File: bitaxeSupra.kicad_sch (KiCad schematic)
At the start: 20 parts, among them J1 54-00164

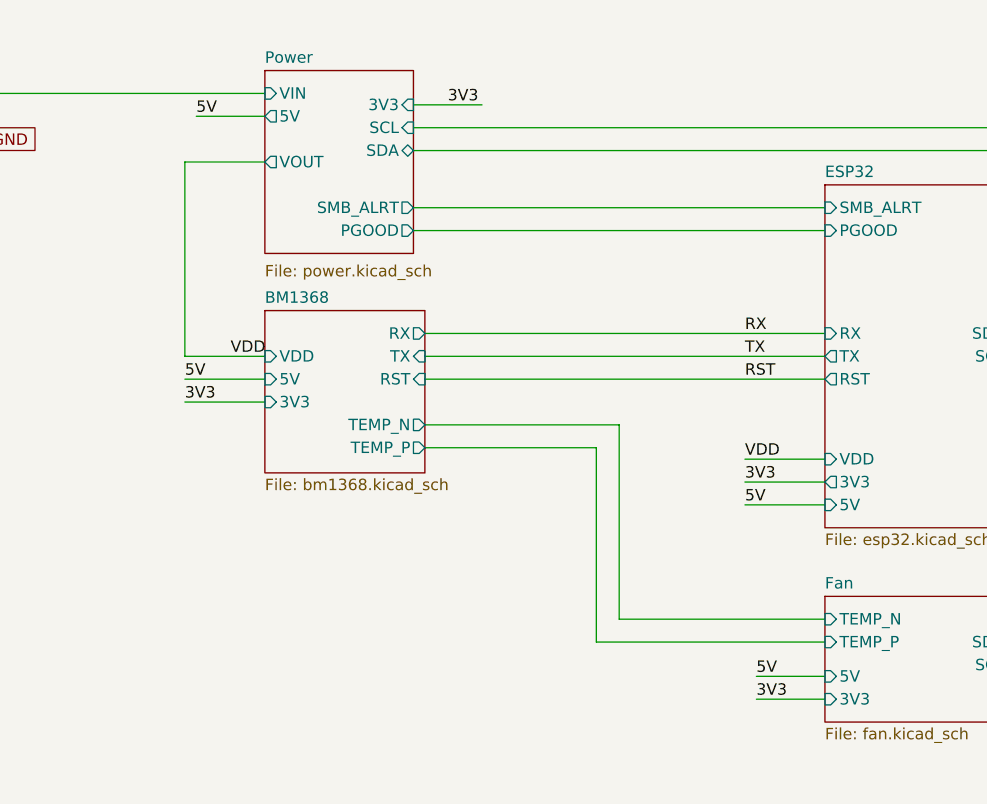
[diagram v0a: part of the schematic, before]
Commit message: changed 1.8V LDO to 1.2V LDO and 25MHz OSC to 1.2V model for #63
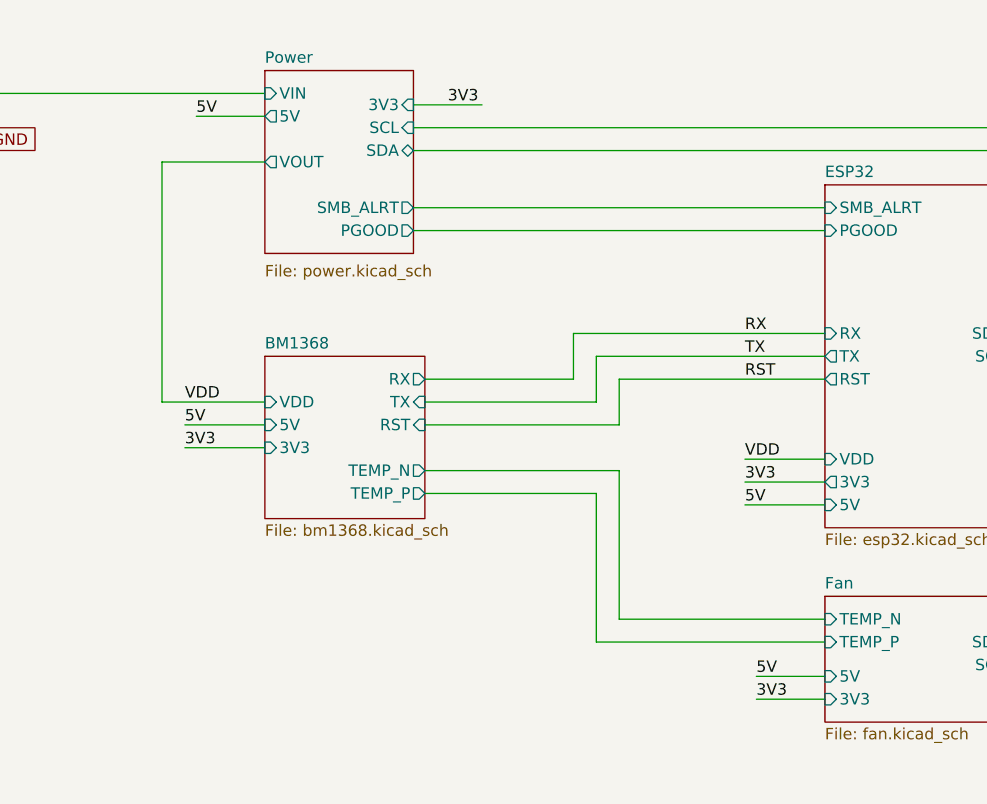
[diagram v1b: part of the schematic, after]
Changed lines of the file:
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@@
 	(wire
 		(pts
-			(xy 130.81 72.39) (xy 175.26 72.39)
+			(xy 147.32 74.93) (xy 147.32 69.85)
+		)
+		(stroke
+			(width 0)
+			(type default)
+		)
+	)
+	(wire
+		(pts
+			(xy 130.81 77.47) (xy 149.86 77.47)
 		)
 		(stroke
@@
 	(wire
 		(pts
+			(xy 152.4 74.93) (xy 175.26 74.93)
+		)
+		(stroke
+			(width 0)
+			(type default)
+		)
+	)
+	(wire
+		(pts
 			(xy 129.54 49.53) (xy 209.55 49.53)
 		)
@@
 	(wire
 		(pts
+			(xy 152.4 80.01) (xy 152.4 74.93)
+		)
+		(stroke
+			(width 0)
+			(type default)
+		)
+	)
+	(wire
+		(pts
 			(xy 35.56 163.83) (xy 35.56 171.45)
 		)
@@
 	(wire
 		(pts
-			(xy 104.14 77.47) (xy 113.03 77.47)
-		)
-		(stroke
-			(width 0)
-			(type default)
-		)
-	)
-	(wire
-		(pts
-			(xy 130.81 69.85) (xy 175.26 69.85)
+			(xy 104.14 82.55) (xy 113.03 82.55)
+		)
+		(stroke
+			(width 0)
+			(type default)
+		)
+	)
+	(wire
+		(pts
+			(xy 130.81 74.93) (xy 147.32 74.93)
 		)
 		(stroke
@@
 	(wire
 		(pts
-			(xy 104.14 72.39) (xy 104.14 50.8)
+			(xy 101.6 77.47) (xy 101.6 50.8)
+		)
+		(stroke
+			(width 0)
+			(type default)
+		)
+	)
+	(wire
+		(pts
+			(xy 130.81 85.09) (xy 152.4 85.09)
+		)
+		(stroke
+			(width 0)
+			(type default)
+		)
+	)
+	(wire
+		(pts
+			(xy 149.86 77.47) (xy 149.86 72.39)
+		)
+		(stroke
+			(width 0)
+			(type default)
+		)
+	)
+	(wire
+		(pts
+			(xy 196.85 106.68) (xy 207.01 106.68)
+		)
+		(stroke
+			(width 0)
+			(type default)
+		)
+	)
+	(wire
+		(pts
+			(xy 104.14 80.01) (xy 113.03 80.01)
+		)
+		(stroke
+			(width 0)
+			(type default)
+		)
+	)
+	(wire
+		(pts
+			(xy 149.86 87.63) (xy 130.81 87.63)
+		)
+		(stroke
+			(width 0)
+			(type default)
+		)
+	)
+	(wire
+		(pts
+			(xy 209.55 104.14) (xy 209.55 69.85)
+		)
+		(stroke
+			(width 0)
+			(type default)
+		)
+	)
+	(wire
+		(pts
+			(xy 129.54 58.42) (xy 175.26 58.42)
+		)
+		(stroke
+			(width 0)
+			(type default)
+		)
+	)
+	(wire
+		(pts
+			(xy 167.64 107.95) (xy 175.26 107.95)
+		)
+		(stroke
+			(width 0)
+			(type default)
+		)
+	)
+	(wire
+		(pts
+			(xy 129.54 55.88) (xy 175.26 55.88)
+		)
+		(stroke
+			(width 0)
+			(type default)
+		)
+	)
+	(wire
+		(pts
+			(xy 35.56 179.07) (xy 35.56 193.04)
+		)
+		(stroke
+			(width 0)
+			(type default)
+		)
+	)
+	(wire
+		(pts
+			(xy 35.56 154.94) (xy 35.56 163.83)
+		)
+		(stroke
+			(width 0)
+			(type default)
+		)
+	)
+	(wire
+		(pts
+			(xy 152.4 85.09) (xy 152.4 101.6)
+		)
+		(stroke
+			(width 0)
+			(type default)
+		)
+	)
+	(wire
+		(pts
+			(xy 147.32 69.85) (xy 175.26 69.85)
+		)
+		(stroke
+			(width 0)
+			(type default)
+		)
+	)
+	(wire
+		(pts
+			(xy 166.37 86.36) (xy 175.26 86.36)
+		)
+		(stroke
+			(width 0)
+			(type default)
+		)
+	)
+	(wire
+		(pts
+			(xy 113.03 77.47) (xy 101.6 77.47)
+		)
+		(stroke
+			(width 0)
+			(type default)
+		)
+	)
+	(wire
+		(pts
+			(xy 101.6 50.8) (xy 113.03 50.8)
 		)
 		(stroke
@@
 	(wire
 		(pts
-			(xy 196.85 106.68) (xy 207.01 106.68)
-		)
-		(stroke
-			(width 0)
-			(type default)
-		)
-	)
-	(wire
-		(pts
-			(xy 104.14 74.93) (xy 113.03 74.93)
-		)
-		(stroke
-			(width 0)
-			(type default)
-		)
-	)
-	(wire
-		(pts
-			(xy 149.86 82.55) (xy 130.81 82.55)
-		)
-		(stroke
-			(width 0)
-			(type default)
-		)
-	)
-	(wire
-		(pts
-			(xy 209.55 104.14) (xy 209.55 69.85)
-		)
-		(stroke
-			(width 0)
-			(type default)
-		)
-	)
-	(wire
-		(pts
-			(xy 129.54 58.42) (xy 175.26 58.42)
-		)
-		(stroke
-			(width 0)
-			(type default)
-		)
-	)
-	(wire
-		(pts
-			(xy 167.64 107.95) (xy 175.26 107.95)
-		)
-		(stroke
-			(width 0)
-			(type default)
-		)
-	)
-	(wire
-		(pts
-			(xy 129.54 55.88) (xy 175.26 55.88)
-		)
-		(stroke
-			(width 0)
-			(type default)
-		)
-	)
-	(wire
-		(pts
-			(xy 35.56 179.07) (xy 35.56 193.04)
-		)
-		(stroke
-			(width 0)
-			(type default)
-		)
-	)
-	(wire
-		(pts
-			(xy 35.56 154.94) (xy 35.56 163.83)
-		)
-		(stroke
-			(width 0)
-			(type default)
-		)
-	)
-	(wire
-		(pts
-			(xy 152.4 80.01) (xy 152.4 101.6)
-		)
-		(stroke
-			(width 0)
-			(type default)
-		)
-	)
-	(wire
-		(pts
-			(xy 166.37 86.36) (xy 175.26 86.36)
-		)
-		(stroke
-			(width 0)
-			(type default)
-		)
-	)
-	(wire
-		(pts
-			(xy 113.03 72.39) (xy 104.14 72.39)
-		)
-		(stroke
-			(width 0)
-			(type default)
-		)
-	)
-	(wire
-		(pts
-			(xy 104.14 50.8) (xy 113.03 50.8)
-		)
-		(stroke
-			(width 0)
-			(type default)
-		)
-	)
-	(wire
-		(pts
-			(xy 130.81 74.93) (xy 175.26 74.93)
+			(xy 149.86 72.39) (xy 175.26 72.39)
 		)
 		(stroke
@@
 	(wire
 		(pts
-			(xy 149.86 104.14) (xy 149.86 82.55)
+			(xy 149.86 104.14) (xy 149.86 87.63)
 		)
 		(stroke
@@
 	)
 	(label "3V3"
-		(at 104.14 77.47 0)
+		(at 104.14 82.55 0)
 		(fields_autoplaced yes)
 		(effects
@@
 	)
 	(label "VDD"
-		(at 109.22 72.39 0)
+		(at 104.14 77.47 0)
 		(fields_autoplaced yes)
 		(effects
@@
 	)
 	(label "5V"
-		(at 104.14 74.93 0)
+		(at 104.14 80.01 0)
 		(fields_autoplaced yes)
 		(effects
@@
 	)
 	(sheet
-		(at 113.03 67.31)
+		(at 113.03 72.39)
 		(size 17.78 18.034)
 		(fields_autoplaced yes)
@@
 		)
 		(property "Sheetname" "BM1368"
-			(at 113.03 66.5984 0)
+			(at 113.03 71.6784 0)
 			(effects
 				(font
@@
 		)
 		(property "Sheetfile" "bm1368.kicad_sch"
-			(at 113.03 85.9286 0)
+			(at 113.03 91.0086 0)
 			(effects
 				(font
@@
 		)
 		(pin "TX" input
-			(at 130.81 72.39 0)
+			(at 130.81 77.47 0)
 			(effects
 				(font
@@
 		)
 		(pin "RX" output
-			(at 130.81 69.85 0)
+			(at 130.81 74.93 0)
 			(effects
 				(font
@@
 		)
 		(pin "RST" input
-			(at 130.81 74.93 0)
+			(at 130.81 80.01 0)
 			(effects
 				(font
@@
 		)
 		(pin "3V3" input
+			(at 113.03 82.55 180)
+			(effects
+				(font
+					(size 1.27 1.27)
+				)
+				(justify left)
+			)
+		)
+		(pin "5V" input
+			(at 113.03 80.01 180)
+			(effects
+				(font
+					(size 1.27 1.27)
+				)
+				(justify left)
+			)
+		)
+		(pin "VDD" input
 			(at 113.03 77.47 180)
 			(effects
@@
 			)
 		)
-		(pin "5V" input
-			(at 113.03 74.93 180)
-			(effects
-				(font
-					(size 1.27 1.27)
-				)
-				(justify left)
-			)
-		)
-		(pin "VDD" input
-			(at 113.03 72.39 180)
-			(effects
-				(font
-					(size 1.27 1.27)
-				)
-				(justify left)
-			)
-		)
 		(pin "TEMP_N" output
-			(at 130.81 80.01 0)
+			(at 130.81 85.09 0)
 			(effects
 				(font
@@
 		)
 		(pin "TEMP_P" output
-			(at 130.81 82.55 0)
-			(effects
-				(font
+			(at 130.81 87.63 0)
+			(effects
+				(font

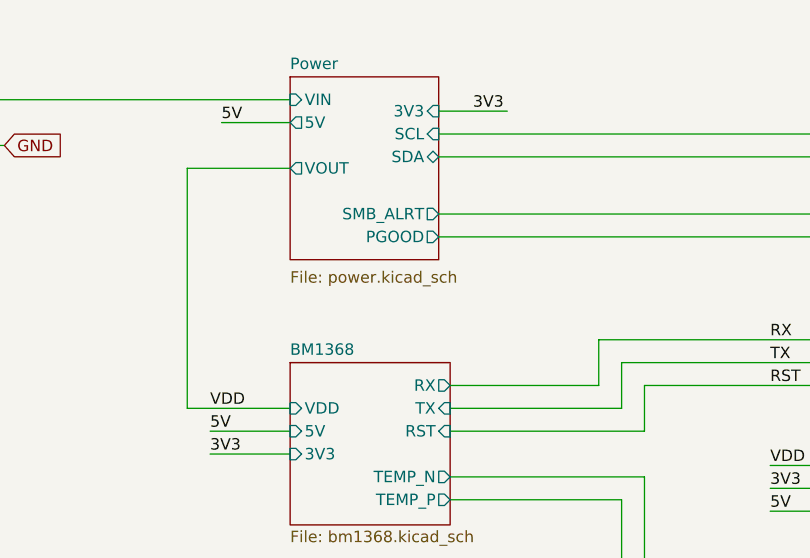
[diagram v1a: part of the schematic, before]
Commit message: started placing TPS546D24A
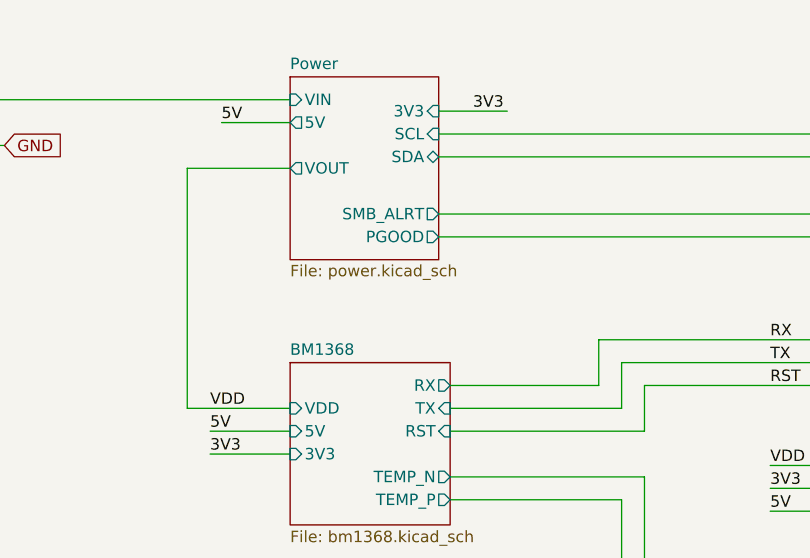
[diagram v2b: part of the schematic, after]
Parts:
- TP12, TP20: footprint TestPoint:TestPoint_Pad_D3.0mm -> TestPoint:TestPoint_Pad_D1.5mm
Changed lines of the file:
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@@
 			)
 		)
-		(property "Footprint" "TestPoint:TestPoint_Pad_D3.0mm"
+		(property "Footprint" "TestPoint:TestPoint_Pad_D1.5mm"
 			(at 85.09 43.18 0)
 			(effects
@@
 			)
 		)
-		(property "Footprint" "TestPoint:TestPoint_Pad_D3.0mm"
+		(property "Footprint" "TestPoint:TestPoint_Pad_D1.5mm"
 			(at 74.93 48.26 0)
 			(effects
@@
 		(at 113.03 40.64)
 		(size 16.51 20.32)
-		(fields_autoplaced yes)
 		(stroke
 			(width 0.1524)
@@
 		)
 		(property "Sheetfile" "power.kicad_sch"
-			(at 113.03 62.1796 0)
-			(effects
-				(font
+			(at 113.03 61.468 0)
+			(effects
+				(font

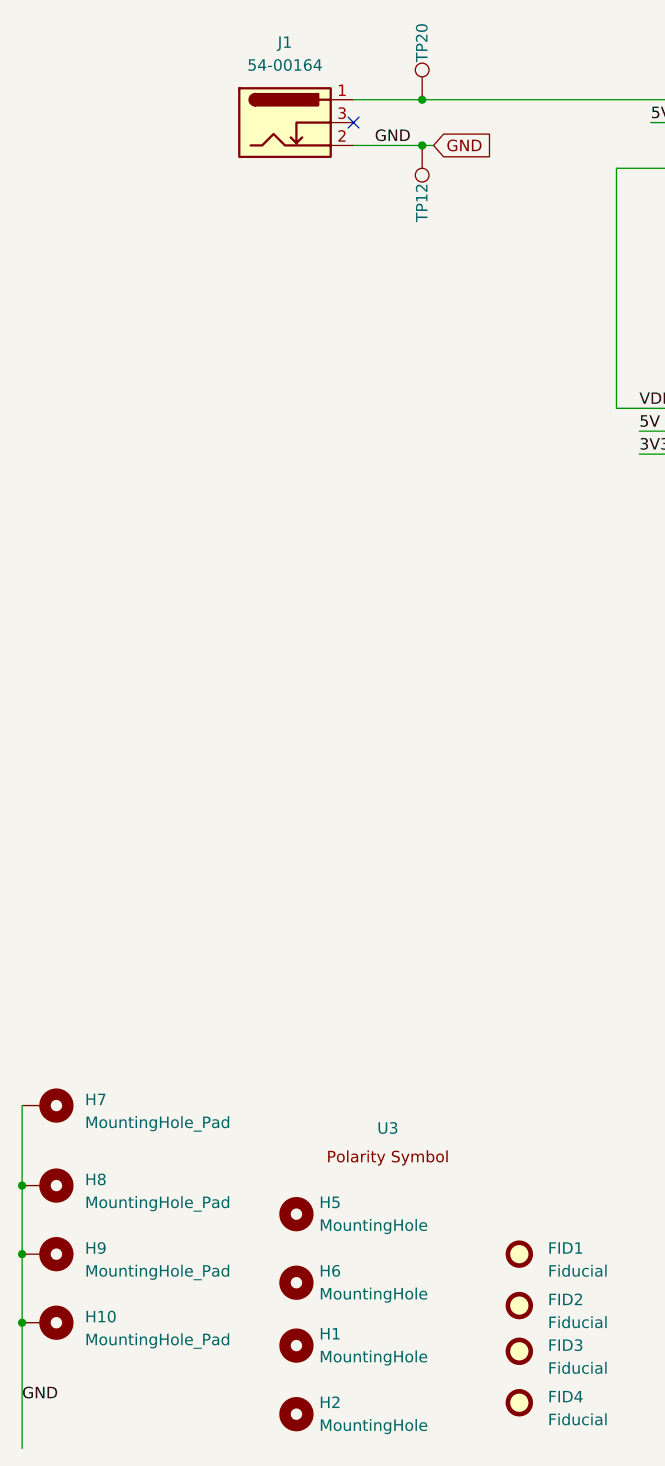
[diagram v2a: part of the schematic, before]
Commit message: mostly routed. still need some power routing
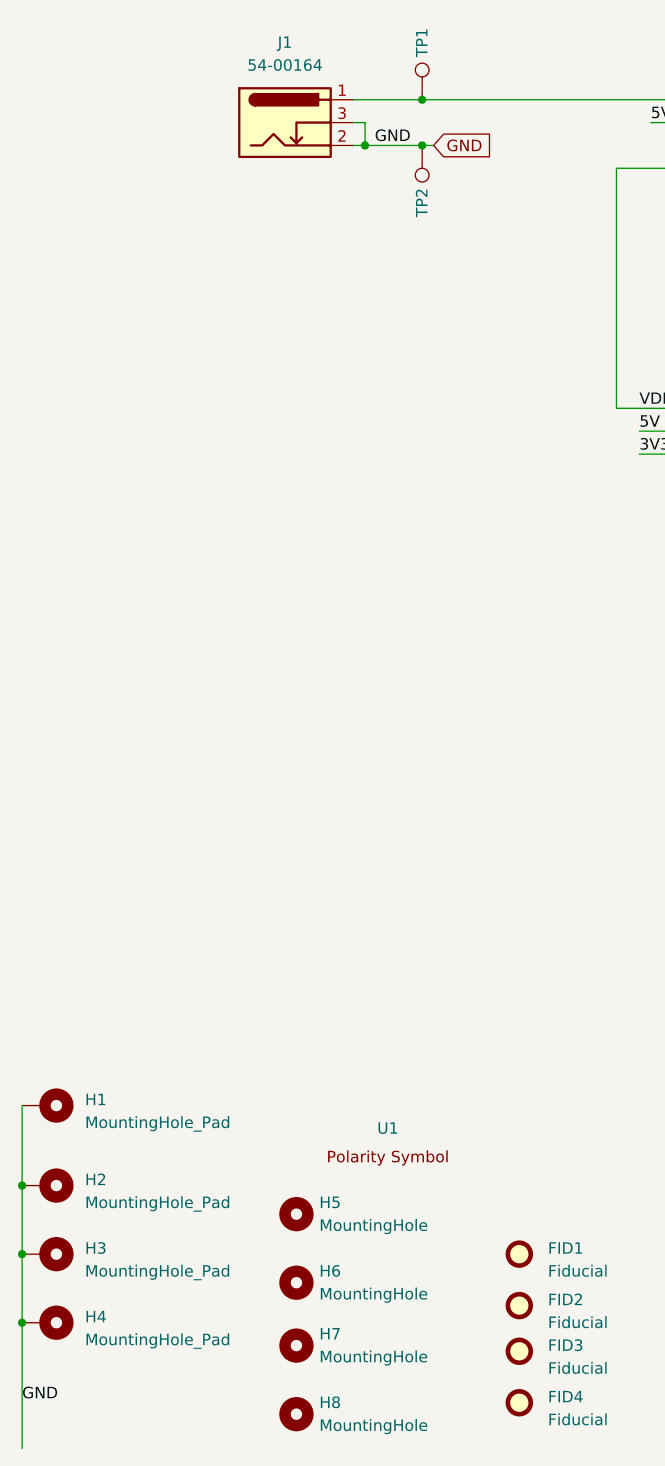
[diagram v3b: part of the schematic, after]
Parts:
- renumbered H7 to H1, H8 to H2, H9 to H3, H10 to H4, H1 to H7, H2 to H8, TP20 to TP1, TP12 to TP2, U3 to U1
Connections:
- net GND: now also J1.3
- no-connect marks 1 -> 0
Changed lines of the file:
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@@
+	)
+	(junction
+		(at 73.66 48.26)
+		(diameter 0)
+		(color 0 0 0 0)
 	)
 	(junction
@@
 		(color 0 0 0 0)
 	)
-	(no_connect
-		(at 72.39 45.72)
+	(wire
+		(pts
+			(xy 73.66 45.72) (xy 73.66 48.26)
+		)
+		(stroke
+			(width 0)
+			(type default)
+		)
 	)
 	(wire
@@
 	(wire
 		(pts
-			(xy 72.39 48.26) (xy 80.01 48.26)
+			(xy 72.39 48.26) (xy 73.66 48.26)
 		)
 		(stroke
@@
 	(wire
 		(pts
+			(xy 73.66 48.26) (xy 80.01 48.26)
+		)
+		(stroke
+			(width 0)
+			(type default)
+		)
+	)
+	(wire
+		(pts
 			(xy 166.37 83.82) (xy 175.26 83.82)
 		)
@@
 		(pts
 			(xy 196.85 104.14) (xy 209.55 104.14)
+		)
+		(stroke
+			(width 0)
+			(type default)
+		)
+	)
+	(wire
+		(pts
+			(xy 72.39 45.72) (xy 73.66 45.72)
 		)
 		(stroke
@@
 		(on_board yes)
 		(dnp no)
-		(property "Reference" "TP20"
+		(property "Reference" "TP1"
 			(at 80.01 36.83 90)
 			(effects
@@
 			(project "bitaxeSupra"
 				(path "/e63e39d7-6ac0-4ffd-8aa3-1841a4541b55"
-					(reference "TP20")
+					(reference "TP1")
 					(unit 1)
 				)
@@
 		(on_board yes)
 		(dnp no)
-		(property "Reference" "TP12"
+		(property "Reference" "TP2"
 			(at 80.01 54.61 90)
 			(effects
@@
 			(project "bitaxeSupra"
 				(path "/e63e39d7-6ac0-4ffd-8aa3-1841a4541b55"
-					(reference "TP12")
+					(reference "TP2")
 					(unit 1)
 				)
@@
 		(dnp no)
 		(fields_autoplaced yes)
-		(property "Reference" "H2"
+		(property "Reference" "H8"
 			(at 68.58 187.9599 0)
 			(effects
@@
 			(project "bitaxeSupra"
 				(path "/e63e39d7-6ac0-4ffd-8aa3-1841a4541b55"
-					(reference "H2")
+					(reference "H8")
 					(unit 1)
 				)
@@
 		(dnp no)
 		(fields_autoplaced yes)
-		(property "Reference" "H7"
+		(property "Reference" "H1"
 			(at 42.545 154.305 90)
 			(effects
@@
 			(project "bitaxeSupra"
 				(path "/e63e39d7-6ac0-4ffd-8aa3-1841a4541b55"
-					(reference "H7")
+					(reference "H1")
 					(unit 1)
 				)
@@
 		(dnp no)
 		(fields_autoplaced yes)
-		(property "Reference" "H1"
+		(property "Reference" "H7"
 			(at 68.58 180.3399 0)
 			(effects
@@
 			(project "bitaxeSupra"
 				(path "/e63e39d7-6ac0-4ffd-8aa3-1841a4541b55"
-					(reference "H1")
+					(reference "H7")
 					(unit 1)
 				)
@@
 		(dnp no)
 		(fields_autoplaced yes)
-		(property "Reference" "H9"
+		(property "Reference" "H3"
 			(at 42.545 170.815 90)
 			(effects
@@
 			(project "bitaxeSupra"
 				(path "/e63e39d7-6ac0-4ffd-8aa3-1841a4541b55"
-					(reference "H9")
+					(reference "H3")
 					(unit 1)
 				)
@@
 		(dnp no)
 		(fields_autoplaced yes)
-		(property "Reference" "H8"
+		(property "Reference" "H2"
 			(at 42.545 163.195 90)
 			(effects
@@
 			(project "bitaxeSupra"
 				(path "/e63e39d7-6ac0-4ffd-8aa3-1841a4541b55"
-					(reference "H8")
+					(reference "H2")
 					(unit 1)
 				)
@@
 		(dnp no)
 		(fields_autoplaced yes)
-		(property "Reference" "H10"
+		(property "Reference" "H4"
 			(at 42.545 178.435 90)
 			(effects
@@
 			(project "bitaxeSupra"
 				(path "/e63e39d7-6ac0-4ffd-8aa3-1841a4541b55"
-					(reference "H10")
+					(reference "H4")
 					(unit 1)
 				)
@@
 		(dnp no)
 		(fields_autoplaced yes)
-		(property "Reference" "U3"
+		(property "Reference" "U1"
 			(at 76.2 157.48 0)
 			(effects
@@
 			(project "bitaxeSupra"
 				(path "/e63e39d7-6ac0-4ffd-8aa3-1841a4541b55"
-					(reference "U3")
+					(reference "U1")
 					(unit 1)
 				)

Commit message: misc
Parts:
- H3: footprint MountingHole:MountingHole_3mm_Pad_Via -> MountingHole:MountingHole_3mm
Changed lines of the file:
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@@
 			)
 		)
-		(property "Footprint" "MountingHole:MountingHole_3mm_Pad_Via"
+		(property "Footprint" "MountingHole:MountingHole_3mm"
 			(at 38.1 171.45 0)
 			(effects
